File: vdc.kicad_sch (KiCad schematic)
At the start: 9 parts, among them IC102 HUC6270

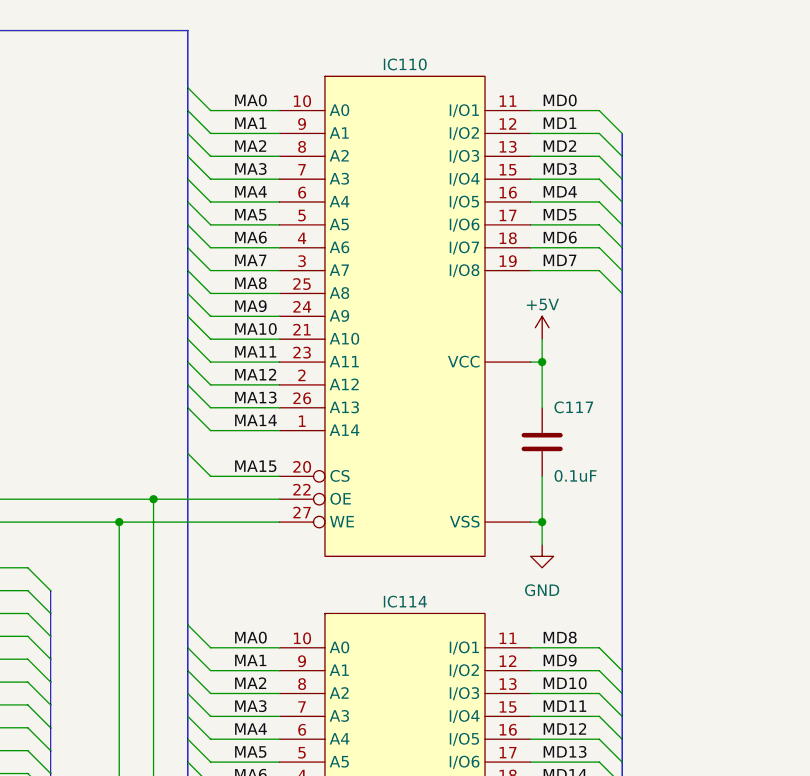
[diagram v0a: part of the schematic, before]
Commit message: Add SMD 1206 footprint and some passives.
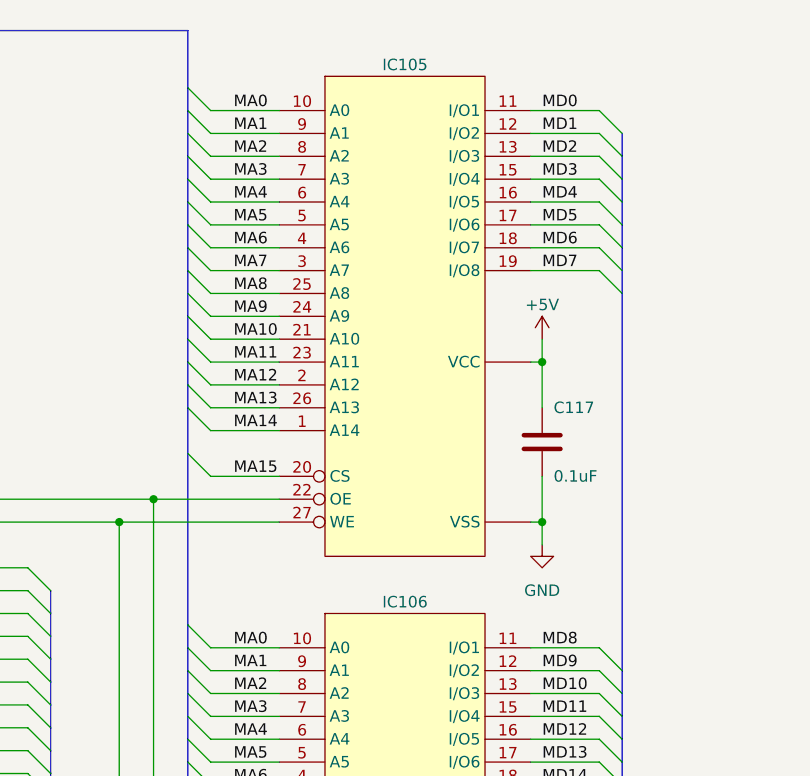
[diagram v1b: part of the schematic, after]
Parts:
- IC105: renamed from IC110; footprint (none) -> A-PCENGINE:HSRM20256LM
- IC106: renamed from IC114; footprint (none) -> A-PCENGINE:HSRM20256LM
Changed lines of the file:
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@@
   (symbol (lib_id "PC-Engine:M20256") (at 261.62 97.79 0) (unit 1)
     (in_bom yes) (on_board yes) (dnp no) (fields_autoplaced)
-    (property "Reference" "IC114" (at 261.62 99.06 0)
+    (property "Reference" "IC106" (at 261.62 99.06 0)
       (effects (font (size 1.27 1.27)))
     )
@@
       (effects (font (size 1.27 1.27)))
     )
-    (property "Footprint" "" (at 261.62 97.79 0)
+    (property "Footprint" "A-PCENGINE:HSRM20256LM" (at 261.62 97.79 0)
       (effects (font (size 1.27 1.27)) hide)
     )
@@
       (project "PCE"
         (path "/c1c718c6-a427-431e-a18b-e46f94ae8e09/ed9120da-14d8-40be-9026-fb246d72bf2f"
-          (reference "IC114") (unit 1)
+          (reference "IC106") (unit 1)
         )
       )
@@
   )
   (symbol (lib_id "PC-Engine:M20256") (at 261.62 38.1 0) (unit 1)
-    (in_bom yes) (on_board yes) (dnp no) (fields_autoplaced)
-    (property "Reference" "IC110" (at 261.62 39.37 0)
+    (in_bom yes) (on_board yes) (dnp no)
+    (property "Reference" "IC105" (at 261.62 39.37 0)
       (effects (font (size 1.27 1.27)))
     )
@@
       (effects (font (size 1.27 1.27)))
     )
-    (property "Footprint" "" (at 261.62 38.1 0)
+    (property "Footprint" "A-PCENGINE:HSRM20256LM" (at 261.62 38.1 0)
       (effects (font (size 1.27 1.27)) hide)
     )
@@
       (project "PCE"
         (path "/c1c718c6-a427-431e-a18b-e46f94ae8e09/ed9120da-14d8-40be-9026-fb246d72bf2f"
-          (reference "IC110") (unit 1)
-        )
-      )
+          (reference "IC105") (unit 1)
+        )
+      )

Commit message: Intermediate save
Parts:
- C102, C104, C105, C106: footprint (none) -> A-PCENGINE:SMD_1206_C
- C129: renamed from C117; footprint (none) -> A-PCENGINE:SMD_1206_C
- C130: renamed from C118; footprint (none) -> A-PCENGINE:SMD_1206_C
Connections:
- net +5V: now also IC105.28 (VCC), IC106.28 (VCC); no longer IC105. (VSS), IC106. (VSS)
- net GND: now also IC105.14 (VSS), IC106.14 (VSS); no longer IC105. (VSS), IC106. (VSS)
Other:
- moved on the sheet: C104
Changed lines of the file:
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@@
   (junction (at 162.56 123.19) (diameter 0) (color 0 0 0 0)
+  )
+  (junction (at 156.21 130.81) (diameter 0) (color 0 0 0 0)
   )
   (junction (at 162.56 130.81) (diameter 0) (color 0 0 0 0)
@@
     (stroke (width 0) (type default))
   )
+  (wire (pts (xy 162.56 143.51) (xy 156.21 143.51))
+    (stroke (width 0) (type default))
+  )
   (wire (pts (xy 209.55 138.43) (xy 201.93 138.43))
     (stroke (width 0) (type default))
@@
     (stroke (width 0) (type default))
   )
+  (wire (pts (xy 156.21 130.81) (xy 156.21 133.35))
+    (stroke (width 0) (type default))
+  )
   (wire (pts (xy 143.51 118.11) (xy 166.37 118.11))
     (stroke (width 0) (type default))
@@
   )
   (wire (pts (xy 218.44 195.58) (xy 218.44 198.12))
+    (stroke (width 0) (type default))
+  )
+  (wire (pts (xy 156.21 143.51) (xy 156.21 140.97))
     (stroke (width 0) (type default))
   )
@@
   (symbol (lib_id "Device:C") (at 276.86 140.97 0) (unit 1)
     (in_bom yes) (on_board yes) (dnp no)
-    (property "Reference" "C118" (at 278.13 137.16 0)
+    (property "Reference" "C130" (at 278.13 137.16 0)
       (effects (font (size 1.27 1.27)) (justify left))
     )
@@
       (effects (font (size 1.27 1.27)) (justify left))
     )
-    (property "Footprint" "" (at 277.8252 144.78 0)
+    (property "Footprint" "A-PCENGINE:SMD_1206_C" (at 277.8252 144.78 0)
       (effects (font (size 1.27 1.27)) hide)
     )
@@
       (project "PCE"
         (path "/c1c718c6-a427-431e-a18b-e46f94ae8e09/ed9120da-14d8-40be-9026-fb246d72bf2f"
-          (reference "C118") (unit 1)
+          (reference "C130") (unit 1)
         )
       )
@@
       (effects (font (size 1.27 1.27)) hide)
     )
-    (pin "")
-    (pin "")
     (pin "1")
     (pin "10")
@@
     (pin "12")
     (pin "13")
+    (pin "14")
     (pin "15")
     (pin "16")
@@
     (pin "26")
     (pin "27")
+    (pin "28")
     (pin "3")
     (pin "4")
@@
       (effects (font (size 1.27 1.27)) (justify left))
     )
-    (property "Footprint" "" (at 232.1052 205.74 0)
+    (property "Footprint" "A-PCENGINE:SMD_1206_C" (at 232.1052 205.74 0)
       (effects (font (size 1.27 1.27)) hide)
     )
@@
   (symbol (lib_id "Device:C") (at 276.86 81.28 0) (unit 1)
     (in_bom yes) (on_board yes) (dnp no)
-    (property "Reference" "C117" (at 278.13 77.47 0)
+    (property "Reference" "C129" (at 278.13 77.47 0)
       (effects (font (size 1.27 1.27)) (justify left))
     )
@@
       (effects (font (size 1.27 1.27)) (justify left))
     )
-    (property "Footprint" "" (at 277.8252 85.09 0)
+    (property "Footprint" "A-PCENGINE:SMD_1206_C" (at 277.8252 85.09 0)
       (effects (font (size 1.27 1.27)) hide)
     )
@@
       (project "PCE"
         (path "/c1c718c6-a427-431e-a18b-e46f94ae8e09/ed9120da-14d8-40be-9026-fb246d72bf2f"
-          (reference "C117") (unit 1)
+          (reference "C129") (unit 1)
         )
       )
@@
       (effects (font (size 1.27 1.27)) (justify left))
     )
-    (property "Footprint" "" (at 244.8052 205.74 0)
+    (property "Footprint" "A-PCENGINE:SMD_1206_C" (at 244.8052 205.74 0)
       (effects (font (size 1.27 1.27)) hide)
     )
@@
     )
   )
-  (symbol (lib_id "Device:C") (at 218.44 201.93 0) (unit 1)
-    (in_bom yes) (on_board yes) (dnp no) (fields_autoplaced)
-    (property "Reference" "C104" (at 222.25 201.295 0)
+  (symbol (lib_id "Device:C") (at 156.21 137.16 0) (mirror y) (unit 1)
+    (in_bom yes) (on_board yes) (dnp no)
+    (property "Reference" "C104" (at 152.4 136.525 0)
       (effects (font (size 1.27 1.27)) (justify left))
     )
-    (property "Value" "0.1uF" (at 222.25 203.835 0)
+    (property "Value" "0.1uF" (at 152.4 139.065 0)
       (effects (font (size 1.27 1.27)) (justify left))
     )
-    (property "Footprint" "" (at 219.4052 205.74 0)
-      (effects (font (size 1.27 1.27)) hide)
-    )
-    (property "Datasheet" "~" (at 218.44 201.93 0)
+    (property "Footprint" "A-PCENGINE:SMD_1206_C" (at 155.2448 140.97 0)
+      (effects (font (size 1.27 1.27)) hide)
+    )
+    (property "Datasheet" "~" (at 156.21 137.16 0)
       (effects (font (size 1.27 1.27)) hide)
     )
@@
       (effects (font (size 1.27 1.27)) hide)
     )
-    (pin "")
-    (pin "")
     (pin "1")
     (pin "10")
@@
     (pin "12")
     (pin "13")
+    (pin "14")
     (pin "15")
     (pin "16")
@@
     (pin "26")
     (pin "27")
+    (pin "28")
     (pin "3")
     (pin "4")
@@
       (effects (font (size 1.27 1.27)) (justify left))
     )
-    (property "Footprint" "" (at 206.7052 205.74 0)
-      (effects (font (size 1.27 1.27)) hide)
-    )
+    (property "Footprint" "A-PCENGINE:SMD_1206_C" (at 206.7052 205.74 0)
+      (effects (font (size 1.27 1.27)) hide)
+    )

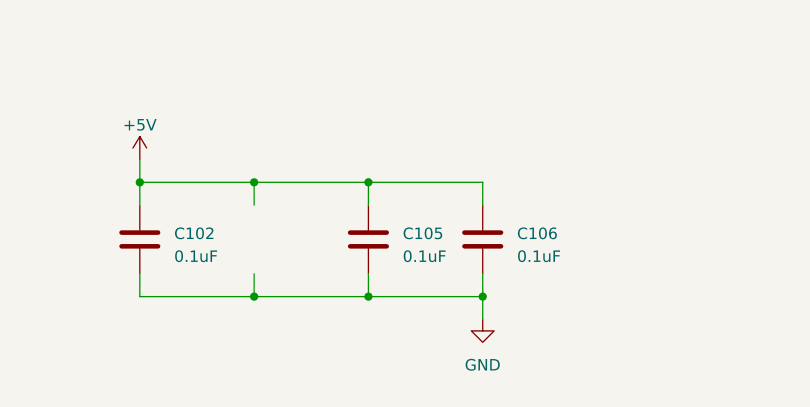
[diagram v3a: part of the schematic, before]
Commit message: Finish basic routing, resolve DRC errors.
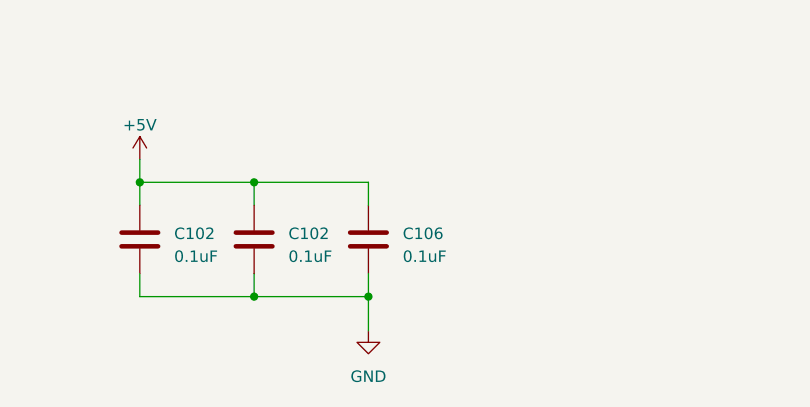
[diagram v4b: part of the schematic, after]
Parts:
- removed C105: 0.1uF, A-PCENGINE:SMD_1206_C, symbol Device:C
- added C102: 0.1uF, A-PCENGINE:SMD_1206_C, symbol Device:C
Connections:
- net +5V: now also C102.1
- net GND: now also C102.2
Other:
- moved on the sheet: C102, C106
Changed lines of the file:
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@@
   (junction (at 233.68 87.63) (diameter 0) (color 0 0 0 0)
   )
-  (junction (at 231.14 195.58) (diameter 0) (color 0 0 0 0)
-  )
   (junction (at 231.14 208.28) (diameter 0) (color 0 0 0 0)
   )
@@
   )
   (junction (at 162.56 138.43) (diameter 0) (color 0 0 0 0)
-  )
-  (junction (at 243.84 208.28) (diameter 0) (color 0 0 0 0)
   )
   (no_connect (at 166.37 82.55))
@@
     (stroke (width 0) (type default))
   )
-  (wire (pts (xy 243.84 195.58) (xy 243.84 198.12))
-    (stroke (width 0) (type default))
-  )
   (wire (pts (xy 166.37 125.73) (xy 162.56 125.73))
     (stroke (width 0) (type default))
@@
     (stroke (width 0) (type default))
   )
-  (wire (pts (xy 243.84 208.28) (xy 231.14 208.28))
-    (stroke (width 0) (type default))
-  )
   (wire (pts (xy 276.86 72.39) (xy 276.86 77.47))
     (stroke (width 0) (type default))
@@
     (stroke (width 0) (type default))
   )
-  (wire (pts (xy 243.84 205.74) (xy 243.84 208.28))
-    (stroke (width 0) (type default))
-  )
   (wire (pts (xy 283.21 119.38) (xy 275.59 119.38))
     (stroke (width 0) (type default))
@@
     (stroke (width 0) (type default))
   )
-  (wire (pts (xy 231.14 195.58) (xy 243.84 195.58))
-    (stroke (width 0) (type default))
-  )
   (wire (pts (xy 201.93 130.81) (xy 219.71 130.81))
     (stroke (width 0) (type default))
@@
     (stroke (width 0) (type default))
   )
-  (wire (pts (xy 243.84 208.28) (xy 243.84 210.82))
+  (wire (pts (xy 231.14 208.28) (xy 231.14 212.09))
     (stroke (width 0) (type default))
   )
@@
     )
   )
-  (symbol (lib_id "Device:C") (at 231.14 201.93 0) (unit 1)
+  (symbol (lib_id "power:GND") (at 276.86 92.71 0) (unit 1)
     (in_bom yes) (on_board yes) (dnp no) (fields_autoplaced)
-    (property "Reference" "C105" (at 234.95 201.295 0)
+    (property "Reference" "#PWR022" (at 276.86 99.06 0)
+      (effects (font (size 1.27 1.27)) hide)
+    )
+    (property "Value" "GND" (at 276.86 97.79 0)
+      (effects (font (size 1.27 1.27)))
+    )
+    (property "Footprint" "" (at 276.86 92.71 0)
+      (effects (font (size 1.27 1.27)) hide)
+    )
+    (property "Datasheet" "" (at 276.86 92.71 0)
+      (effects (font (size 1.27 1.27)) hide)
+    )
+    (pin "1")
+    (instances
+      (project "PCE"
+        (path "/c1c718c6-a427-431e-a18b-e46f94ae8e09/ed9120da-14d8-40be-9026-fb246d72bf2f"
+          (reference "#PWR022") (unit 1)
+        )
+      )
+    )
+  )
+  (symbol (lib_id "Device:C") (at 205.74 201.93 0) (unit 1)
+    (in_bom yes) (on_board yes) (dnp no) (fields_autoplaced)
+    (property "Reference" "C102" (at 209.55 201.295 0)
       (effects (font (size 1.27 1.27)) (justify left))
     )
-    (property "Value" "0.1uF" (at 234.95 203.835 0)
+    (property "Value" "0.1uF" (at 209.55 203.835 0)
       (effects (font (size 1.27 1.27)) (justify left))
     )
-    (property "Footprint" "A-PCENGINE:SMD_1206_C" (at 232.1052 205.74 0)
-      (effects (font (size 1.27 1.27)) hide)
-    )
-    (property "Datasheet" "~" (at 231.14 201.93 0)
+    (property "Footprint" "A-PCENGINE:SMD_1206_C" (at 206.7052 205.74 0)
+      (effects (font (size 1.27 1.27)) hide)
+    )
+    (property "Datasheet" "~" (at 205.74 201.93 0)
       (effects (font (size 1.27 1.27)) hide)
     )
@@
       (project "PCE"
         (path "/c1c718c6-a427-431e-a18b-e46f94ae8e09/1d91d06a-381a-4a70-bfc1-2abf4d159a91"
-          (reference "C105") (unit 1)
+          (reference "C102") (unit 1)
         )
         (path "/c1c718c6-a427-431e-a18b-e46f94ae8e09/ed9120da-14d8-40be-9026-fb246d72bf2f"
-          (reference "C124") (unit 1)
-        )
-      )
-    )
-  )
-  (symbol (lib_id "power:GND") (at 276.86 92.71 0) (unit 1)
-    (in_bom yes) (on_board yes) (dnp no) (fields_autoplaced)
-    (property "Reference" "#PWR022" (at 276.86 99.06 0)
-      (effects (font (size 1.27 1.27)) hide)
-    )
-    (property "Value" "GND" (at 276.86 97.79 0)
-      (effects (font (size 1.27 1.27)))
-    )
-    (property "Footprint" "" (at 276.86 92.71 0)
-      (effects (font (size 1.27 1.27)) hide)
-    )
-    (property "Datasheet" "" (at 276.86 92.71 0)
-      (effects (font (size 1.27 1.27)) hide)
-    )
-    (pin "1")
-    (instances
-      (project "PCE"
-        (path "/c1c718c6-a427-431e-a18b-e46f94ae8e09/ed9120da-14d8-40be-9026-fb246d72bf2f"
-          (reference "#PWR022") (unit 1)
+          (reference "C125") (unit 1)
         )
       )
@@
     )
   )
-  (symbol (lib_id "Device:C") (at 243.84 201.93 0) (unit 1)
+  (symbol (lib_id "Device:C") (at 231.14 201.93 0) (unit 1)
     (in_bom yes) (on_board yes) (dnp no)
-    (property "Reference" "C106" (at 247.65 201.295 0)
+    (property "Reference" "C106" (at 234.95 201.295 0)
       (effects (font (size 1.27 1.27)) (justify left))
     )
-    (property "Value" "0.1uF" (at 247.65 203.835 0)
+    (property "Value" "0.1uF" (at 234.95 203.835 0)
       (effects (font (size 1.27 1.27)) (justify left))
     )
-    (property "Footprint" "A-PCENGINE:SMD_1206_C" (at 244.8052 205.74 0)
-      (effects (font (size 1.27 1.27)) hide)
-    )
-    (property "Datasheet" "~" (at 243.84 201.93 0)
+    (property "Footprint" "A-PCENGINE:SMD_1206_C" (at 232.1052 205.74 0)
+      (effects (font (size 1.27 1.27)) hide)
+    )
+    (property "Datasheet" "~" (at 231.14 201.93 0)
       (effects (font (size 1.27 1.27)) hide)
     )
@@
         )
         (path "/c1c718c6-a427-431e-a18b-e46f94ae8e09/ed9120da-14d8-40be-9026-fb246d72bf2f"
-          (reference "C121") (unit 1)
+          (reference "C124") (unit 1)
         )
       )
     )
   )
-  (symbol (lib_id "power:GND") (at 243.84 210.82 0) (unit 1)
+  (symbol (lib_id "power:GND") (at 231.14 212.09 0) (unit 1)
     (in_bom yes) (on_board yes) (dnp no) (fields_autoplaced)
-    (property "Reference" "#PWR07" (at 243.84 217.17 0)
-      (effects (font (size 1.27 1.27)) hide)
-    )
-    (property "Value" "GND" (at 243.84 215.9 0)
+    (property "Reference" "#PWR07" (at 231.14 218.44 0)
+      (effects (font (size 1.27 1.27)) hide)
+    )
+    (property "Value" "GND" (at 231.14 217.17 0)
       (effects (font (size 1.27 1.27)))
     )
-    (property "Footprint" "" (at 243.84 210.82 0)
-      (effects (font (size 1.27 1.27)) hide)
-    )
-    (property "Datasheet" "" (at 243.84 210.82 0)
+    (property "Footprint" "" (at 231.14 212.09 0)
+      (effects (font (size 1.27 1.27)) hide)
+    )
+    (property "Datasheet" "" (at 231.14 212.09 0)
       (effects (font (size 1.27 1.27)) hide)
     )
@@
     )
   )
-  (symbol (lib_id "Device:C") (at 205.74 201.93 0) (unit 1)
+  (symbol (lib_id "Device:C") (at 218.44 201.93 0) (unit 1)
     (in_bom yes) (on_board yes) (dnp no) (fields_autoplaced)
-    (property "Reference" "C102" (at 209.55 201.295 0)
+    (property "Reference" "C102" (at 222.25 201.295 0)
       (effects (font (size 1.27 1.27)) (justify left))
     )
-    (property "Value" "0.1uF" (at 209.55 203.835 0)
+    (property "Value" "0.1uF" (at 222.25 203.835 0)
       (effects (font (size 1.27 1.27)) (justify left))
     )
-    (property "Footprint" "A-PCENGINE:SMD_1206_C" (at 206.7052 205.74 0)
-      (effects (font (size 1.27 1.27)) hide)
-    )
-    (property "Datasheet" "~" (at 205.74 201.93 0)
+    (property "Footprint" "A-PCENGINE:SMD_1206_C" (at 219.4052 205.74 0)
+      (effects (font (size 1.27 1.27)) hide)
+    )
+    (property "Datasheet" "~" (at 218.44 201.93 0)
       (effects (font (size 1.27 1.27)) hide)
     )
@@
         )
         (path "/c1c718c6-a427-431e-a18b-e46f94ae8e09/ed9120da-14d8-40be-9026-fb246d72bf2f"
-          (reference "C120") (unit 1)
+          (reference "C126") (unit 1)
         )
       )
